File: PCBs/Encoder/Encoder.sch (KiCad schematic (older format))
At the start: 3 parts, among them J1 Conn_01x06_Male, U1 AS5047D

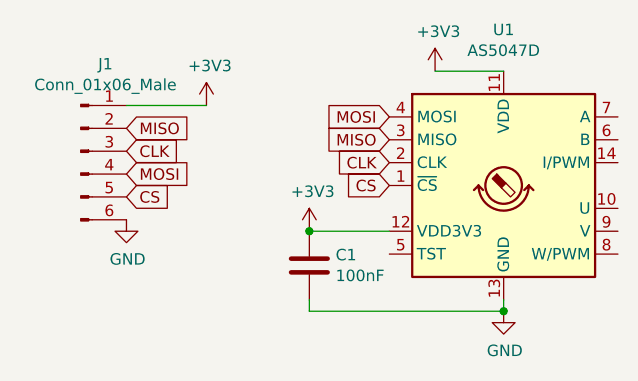
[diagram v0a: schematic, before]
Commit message: J0 stls
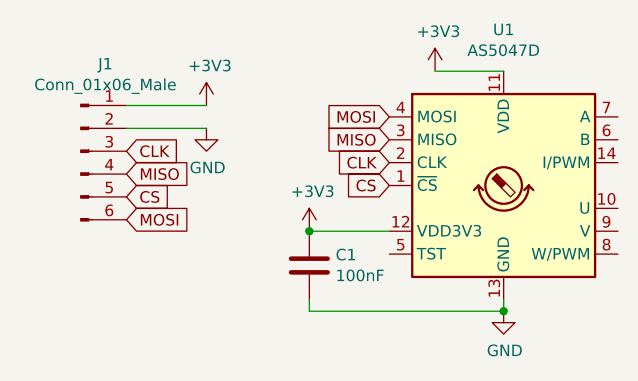
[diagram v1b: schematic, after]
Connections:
- net GND: now also J1.2 (Pin_2); no longer J1.6 (Pin_6)
- net MISO: now also J1.4 (Pin_4); no longer J1.2 (Pin_2)
- net MOSI: now also J1.6 (Pin_6); no longer J1.4 (Pin_4)
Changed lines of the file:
@@
 Wire Wire Line
 	4400 3450 4050 3450
+Text GLabel 4050 3950 2    50   Input ~ 0
+MOSI
 Text GLabel 4050 3750 2    50   Input ~ 0
-MOSI
-Text GLabel 4050 3550 2    50   Input ~ 0
 MISO
 Text GLabel 4050 3650 2    50   Input ~ 0
@@
 L power:GND #PWR01
 U 1 1 60A24D56
-P 4050 3950
-F 0 "#PWR01" H 4050 3700 50  0001 C CNN
-F 1 "GND" H 4055 3777 50  0000 C CNN
-F 2 "" H 4050 3950 50  0001 C CNN
-F 3 "" H 4050 3950 50  0001 C CNN
-	1    4050 3950
+P 4400 3550
+F 0 "#PWR01" H 4400 3300 50  0001 C CNN
+F 1 "GND" H 4405 3377 50  0000 C CNN
+F 2 "" H 4400 3550 50  0001 C CNN
+F 3 "" H 4400 3550 50  0001 C CNN
+	1    4400 3550
 	1    0    0    -1
 $EndComp
@@
 	1    0    0    -1
 $EndComp
+Wire Wire Line
+	4400 3550 4050 3550
 $EndSCHEMATC
